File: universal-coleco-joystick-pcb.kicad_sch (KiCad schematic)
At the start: 45 parts, among them J1 Sanwa Joystick, J2 DE9_Receptacle, J3 Conn_01x09_Socket, SW1 Arm, SW10 2, SW11 #, SW12 9, SW13 6, SW14 3, SW2 Fire, SW3 *, SW4 7, SW5 1, SW6 4, SW7 0, SW8 8, SW9 5

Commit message: Diode soup
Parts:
- D1, D10, D11, D12, D13, D14, D15, D16, D17, D18, D19, D2, D20, D21, D22, D23, D24, D25, D26, D27, D28, D3, D4, D5, D6, D7, D8, D9: footprint (none) -> Diode_THT:D_DO-41_SOD81_P10.16mm_Horizontal
- J1: footprint (none) -> Connector_PinHeader_2.54mm:PinHeader_1x05_P2.54mm_Vertical
- J2: footprint (none) -> Connector_Dsub:DSUB-9_Female_Horizontal_P2.77x2.84mm_EdgePinOffset7.70mm_Housed_MountingHolesOffset9.12mm
- J3: footprint (none) -> Connector_PinHeader_2.54mm:PinHeader_1x09_P2.54mm_Vertical
- SW10, SW11, SW12, SW13, SW14, SW3, SW4, SW5, SW6, SW7, SW8, SW9: footprint (none) -> Connector_PinHeader_2.54mm:PinHeader_1x02_P2.54mm_Vertical
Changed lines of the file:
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@@
 			)
 		)
-		(property "Footprint" ""
+		(property "Footprint" "Diode_THT:D_DO-41_SOD81_P10.16mm_Horizontal"
 			(at 210.82 55.88 0)
 			(effects
@@
 			)
 		)
-		(property "Footprint" ""
+		(property "Footprint" "Diode_THT:D_DO-41_SOD81_P10.16mm_Horizontal"
 			(at 218.44 93.98 0)
 			(effects
@@
 			)
 		)
-		(property "Footprint" ""
+		(property "Footprint" "Diode_THT:D_DO-41_SOD81_P10.16mm_Horizontal"
 			(at 85.09 58.42 90)
 			(effects
@@
 			)
 		)
-		(property "Footprint" ""
+		(property "Footprint" "Diode_THT:D_DO-41_SOD81_P10.16mm_Horizontal"
 			(at 210.82 63.5 0)
 			(effects
@@
 			)
 		)
-		(property "Footprint" ""
+		(property "Footprint" "Diode_THT:D_DO-41_SOD81_P10.16mm_Horizontal"
 			(at 226.06 71.12 0)
 			(effects
@@
 			)
 		)
-		(property "Footprint" ""
+		(property "Footprint" "Diode_THT:D_DO-41_SOD81_P10.16mm_Horizontal"
 			(at 226.06 40.64 0)
 			(effects
@@
 			)
 		)
-		(property "Footprint" ""
+		(property "Footprint" "Diode_THT:D_DO-41_SOD81_P10.16mm_Horizontal"
 			(at 226.06 33.02 0)
 			(effects
@@
 			)
 		)
-		(property "Footprint" ""
+		(property "Footprint" "Diode_THT:D_DO-41_SOD81_P10.16mm_Horizontal"
 			(at 85.09 55.88 90)
 			(effects
@@
 			)
 		)
-		(property "Footprint" ""
+		(property "Footprint" "Diode_THT:D_DO-41_SOD81_P10.16mm_Horizontal"
 			(at 218.44 78.74 0)
 			(effects
@@
 			)
 		)
-		(property "Footprint" ""
+		(property "Footprint" "Diode_THT:D_DO-41_SOD81_P10.16mm_Horizontal"
 			(at 210.82 33.02 0)
 			(effects
@@
 			)
 		)
-		(property "Footprint" ""
+		(property "Footprint" "Connector_PinHeader_2.54mm:PinHeader_1x02_P2.54mm_Vertical"
 			(at 189.23 76.2 0)
 			(effects
@@
 			)
 		)
-		(property "Footprint" ""
+		(property "Footprint" "Connector_PinHeader_2.54mm:PinHeader_1x02_P2.54mm_Vertical"
 			(at 189.23 68.58 0)
 			(effects
@@
 			)
 		)
-		(property "Footprint" ""
+		(property "Footprint" "Connector_PinHeader_2.54mm:PinHeader_1x05_P2.54mm_Vertical"
 			(at 66.04 58.42 0)
 			(effects
@@
 			)
 		)
-		(property "Footprint" ""
+		(property "Footprint" "Diode_THT:D_DO-41_SOD81_P10.16mm_Horizontal"
 			(at 218.44 40.64 0)
 			(effects
@@
 			)
 		)
-		(property "Footprint" ""
+		(property "Footprint" "Connector_PinHeader_2.54mm:PinHeader_1x02_P2.54mm_Vertical"
 			(at 189.23 114.3 0)
 			(effects
@@
 			)
 		)
-		(property "Footprint" ""
+		(property "Footprint" "Connector_PinHeader_2.54mm:PinHeader_1x02_P2.54mm_Vertical"
 			(at 189.23 91.44 0)
 			(effects
@@
 			)
 		)
-		(property "Footprint" ""
+		(property "Footprint" "Connector_Dsub:DSUB-9_Female_Horizontal_P2.77x2.84mm_EdgePinOffset7.70mm_Housed_MountingHolesOffset9.12mm"
 			(at 96.52 143.51 0)
 			(effects
@@
 			)
 		)
-		(property "Footprint" ""
+		(property "Footprint" "Diode_THT:D_DO-41_SOD81_P10.16mm_Horizontal"
 			(at 80.01 78.74 90)
 			(effects
@@
 			)
 		)
-		(property "Footprint" ""
+		(property "Footprint" "Diode_THT:D_DO-41_SOD81_P10.16mm_Horizontal"
 			(at 203.2 109.22 0)
 			(effects
@@
 			)
 		)
-		(property "Footprint" ""
+		(property "Footprint" "Diode_THT:D_DO-41_SOD81_P10.16mm_Horizontal"
 			(at 226.06 116.84 0)
 			(effects
@@
 			)
 		)
-		(property "Footprint" ""
+		(property "Footprint" "Diode_THT:D_DO-41_SOD81_P10.16mm_Horizontal"
 			(at 218.44 71.12 0)
 			(effects
@@
 			)
 		)
-		(property "Footprint" ""
+		(property "Footprint" "Connector_PinHeader_2.54mm:PinHeader_1x09_P2.54mm_Vertical"
 			(at 48.26 163.83 0)
 			(effects
@@
 			)
 		)
-		(property "Footprint" ""
+		(property "Footprint" "Diode_THT:D_DO-41_SOD81_P10.16mm_Horizontal"
 			(at 210.82 71.12 0)
 			(effects
@@
 			)
 		)
-		(property "Footprint" ""
+		(property "Footprint" "Diode_THT:D_DO-41_SOD81_P10.16mm_Horizontal"
 			(at 218.44 86.36 0)
 			(effects
@@
 			)
 		)
-		(property "Footprint" ""
+		(property "Footprint" "Connector_PinHeader_2.54mm:PinHeader_1x02_P2.54mm_Vertical"
 			(at 189.23 106.68 0)
 			(effects
@@
 			)
 		)
-		(property "Footprint" ""
+		(property "Footprint" "Diode_THT:D_DO-41_SOD81_P10.16mm_Horizontal"
 			(at 218.44 55.88 0)
 			(effects
@@
 			)
 		)
-		(property "Footprint" ""
+		(property "Footprint" "Connector_PinHeader_2.54mm:PinHeader_1x02_P2.54mm_Vertical"
 			(at 189.23 53.34 0)
 			(effects
@@
 			)
 		)
-		(property "Footprint" ""
+		(property "Footprint" "Connector_PinHeader_2.54mm:PinHeader_1x02_P2.54mm_Vertical"
 			(at 189.23 60.96 0)
 			(effects
@@
 			)
 		)
-		(property "Footprint" ""
+		(property "Footprint" "Diode_THT:D_DO-41_SOD81_P10.16mm_Horizontal"
 			(at 210.82 78.74 0)
 			(effects
@@
 			)
 		)
-		(property "Footprint" ""
+		(property "Footprint" "Diode_THT:D_DO-41_SOD81_P10.16mm_Horizontal"
 			(at 85.09 60.96 90)
 			(effects
@@
 			)
 		)
-		(property "Footprint" ""
+		(property "Footprint" "Diode_THT:D_DO-41_SOD81_P10.16mm_Horizontal"
 			(at 226.06 48.26 0)
 			(effects
@@
 			)
 		)
-		(property "Footprint" ""
+		(property "Footprint" "Diode_THT:D_DO-41_SOD81_P10.16mm_Horizontal"
 			(at 203.2 116.84 0)
 			(effects
@@
 			)
 		)
-		(property "Footprint" ""
+		(property "Footprint" "Diode_THT:D_DO-41_SOD81_P10.16mm_Horizontal"
 			(at 80.01 91.44 90)
 			(effects
@@
 			)
 		)
-		(property "Footprint" ""
+		(property "Footprint" "Diode_THT:D_DO-41_SOD81_P10.16mm_Horizontal"
 			(at 85.09 53.34 90)
 			(effects
@@
 			)
 		)
-		(property "Footprint" ""
+		(property "Footprint" "Diode_THT:D_DO-41_SOD81_P10.16mm_Horizontal"
 			(at 210.82 101.6 0)
 			(effects
@@
 			)
 		)
-		(property "Footprint" ""
+		(property "Footprint" "Connector_PinHeader_2.54mm:PinHeader_1x02_P2.54mm_Vertical"
 			(at 189.23 38.1 0)
 			(effects
@@
 			)
 		)
-		(property "Footprint" ""
+		(property "Footprint" "Connector_PinHeader_2.54mm:PinHeader_1x02_P2.54mm_Vertical"
 			(at 189.23 83.82 0)
 			(effects
@@
 			)
 		)
-		(property "Footprint" ""
+		(property "Footprint" "Diode_THT:D_DO-41_SOD81_P10.16mm_Horizontal"
 			(at 203.2 63.5 0)
 			(effects
@@
 			)
 		)
-		(property "Footprint" ""
+		(property "Footprint" "Diode_THT:D_DO-41_SOD81_P10.16mm_Horizontal"
 			(at 203.2 93.98 0)
 			(effects
@@
 			)
 		)
-		(property "Footprint" ""
+		(property "Footprint" "Connector_PinHeader_2.54mm:PinHeader_1x02_P2.54mm_Vertical"
 			(at 189.23 99.06 0)
 			(effects
@@
 			)
 		)
-		(property "Footprint" ""
+		(property "Footprint" "Connector_PinHeader_2.54mm:PinHeader_1x02_P2.54mm_Vertical"
 			(at 189.23 30.48 0)
 			(effects
@@
 			)
 		)
-		(property "Footprint" ""
+		(property "Footprint" "Diode_THT:D_DO-41_SOD81_P10.16mm_Horizontal"
 			(at 203.2 55.88 0)
 			(effects
@@
 			)
 		)
-		(property "Footprint" ""
+		(property "Footprint" "Connector_PinHeader_2.54mm:PinHeader_1x02_P2.54mm_Vertical"
 			(at 189.23 45.72 0)
 			(effects

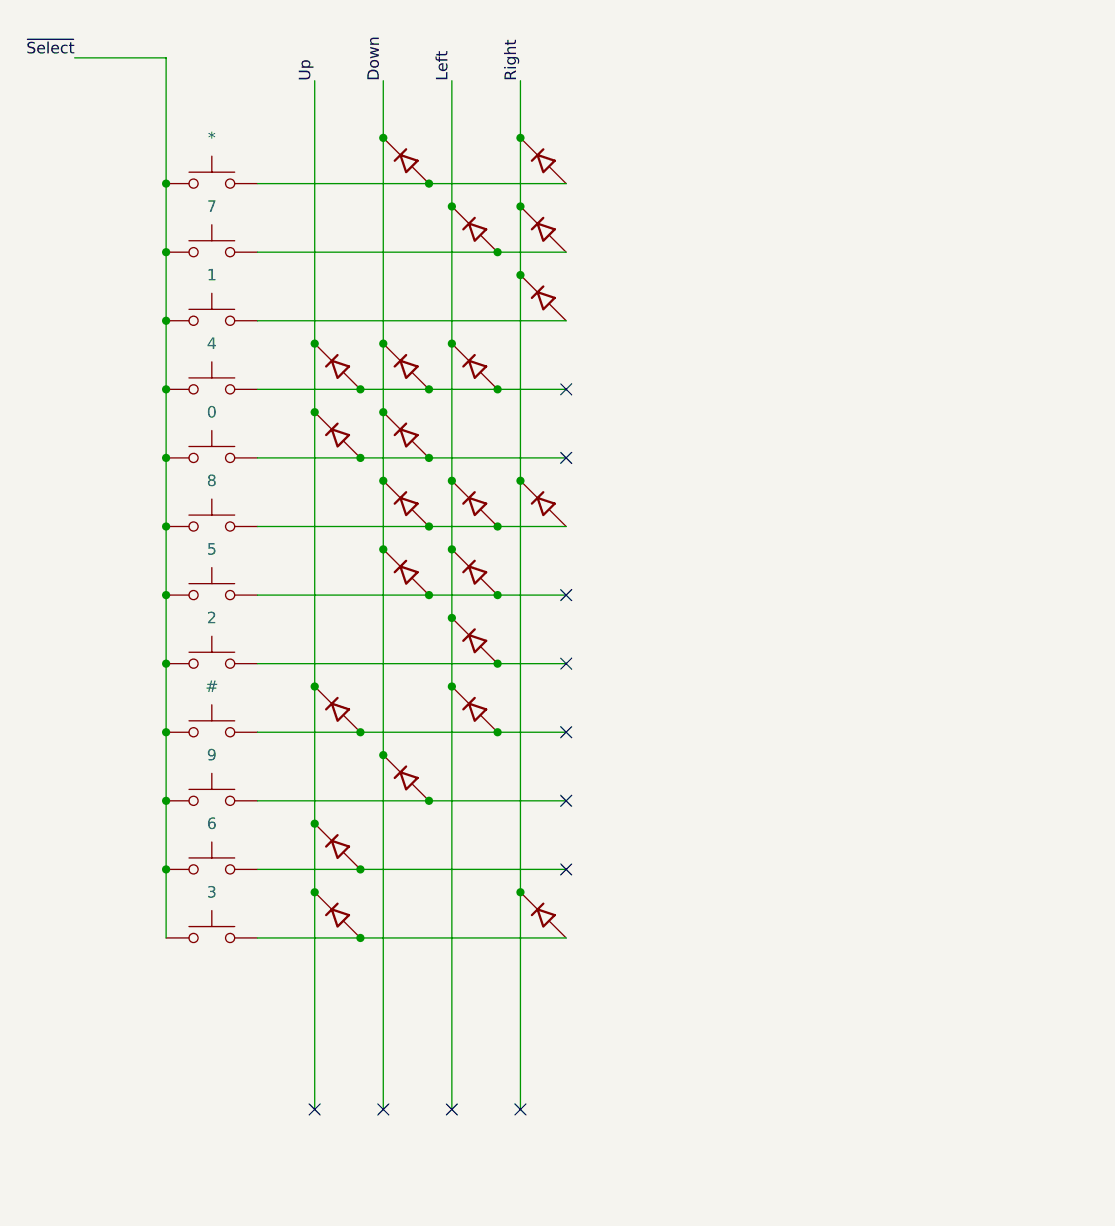
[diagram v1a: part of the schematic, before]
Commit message: Linear KP header
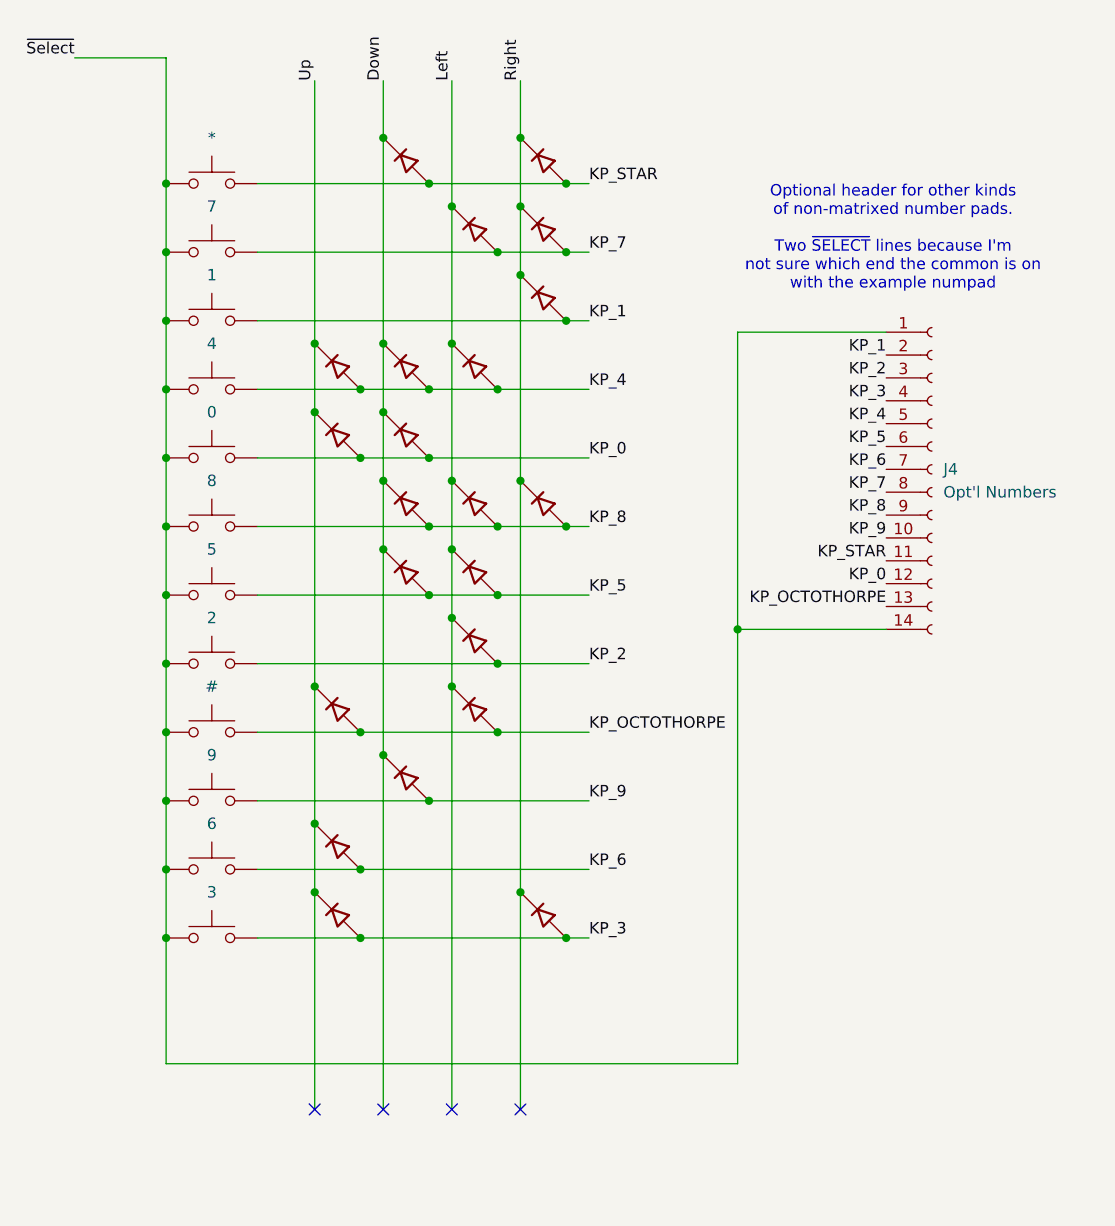
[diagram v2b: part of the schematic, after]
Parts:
- added J4: Opt'l Numbers, Connector_PinHeader_2.54mm:PinHeader_1x14_P2.54mm_Vertical, symbol Connector:Conn_01x14_Socket
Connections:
- net ~{Select}: now also J4.1 (Pin_1), J4.14 (Pin_14)
- net KP_4: now reaches D12.2 (A), D13.2 (A), D14.2 (A), SW6.2
- net KP_4: now also J4.5 (Pin_5)
- net KP_OCTOTHORPE: now reaches D23.2 (A), D24.2 (A), SW11.2
- net KP_OCTOTHORPE: now also J4.13 (Pin_13)
- net KP_0: now reaches D15.2 (A), D16.2 (A), SW7.2
- net KP_0: now also J4.12 (Pin_12)
- net KP_8: now reaches D17.2 (A), D18.2 (A), D19.2 (A), SW8.2
- net KP_8: now also J4.9 (Pin_9)
- net KP_7: now reaches D10.2 (A), D9.2 (A), SW4.2
- net KP_7: now also J4.8 (Pin_8)
- net KP_STAR: now reaches D7.2 (A), D8.2 (A), SW3.2
- net KP_STAR: now also J4.11 (Pin_11)
- net KP_5: now reaches D20.2 (A), D21.2 (A), SW9.2
- net KP_5: now also J4.6 (Pin_6)
- net KP_3: now reaches D27.2 (A), D28.2 (A), SW14.2
- net KP_3: now also J4.4 (Pin_4)
- net KP_6: now reaches D26.2 (A), SW13.2
- net KP_6: now also J4.7 (Pin_7)
- net KP_2: now reaches D22.2 (A), SW10.2
- net KP_2: now also J4.3 (Pin_3)
- net KP_1: now reaches D11.2 (A), SW5.2
- net KP_1: now also J4.2 (Pin_2)
- net KP_9: now reaches D25.2 (A), SW12.2
- net KP_9: now also J4.10 (Pin_10)
- no-connect marks 11 -> 4
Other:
- note added: "Optional header for other kinds of non-matrixed number pads. Two ~{SELECT} lines because I'm not sure which end the common is on with the example numpad"

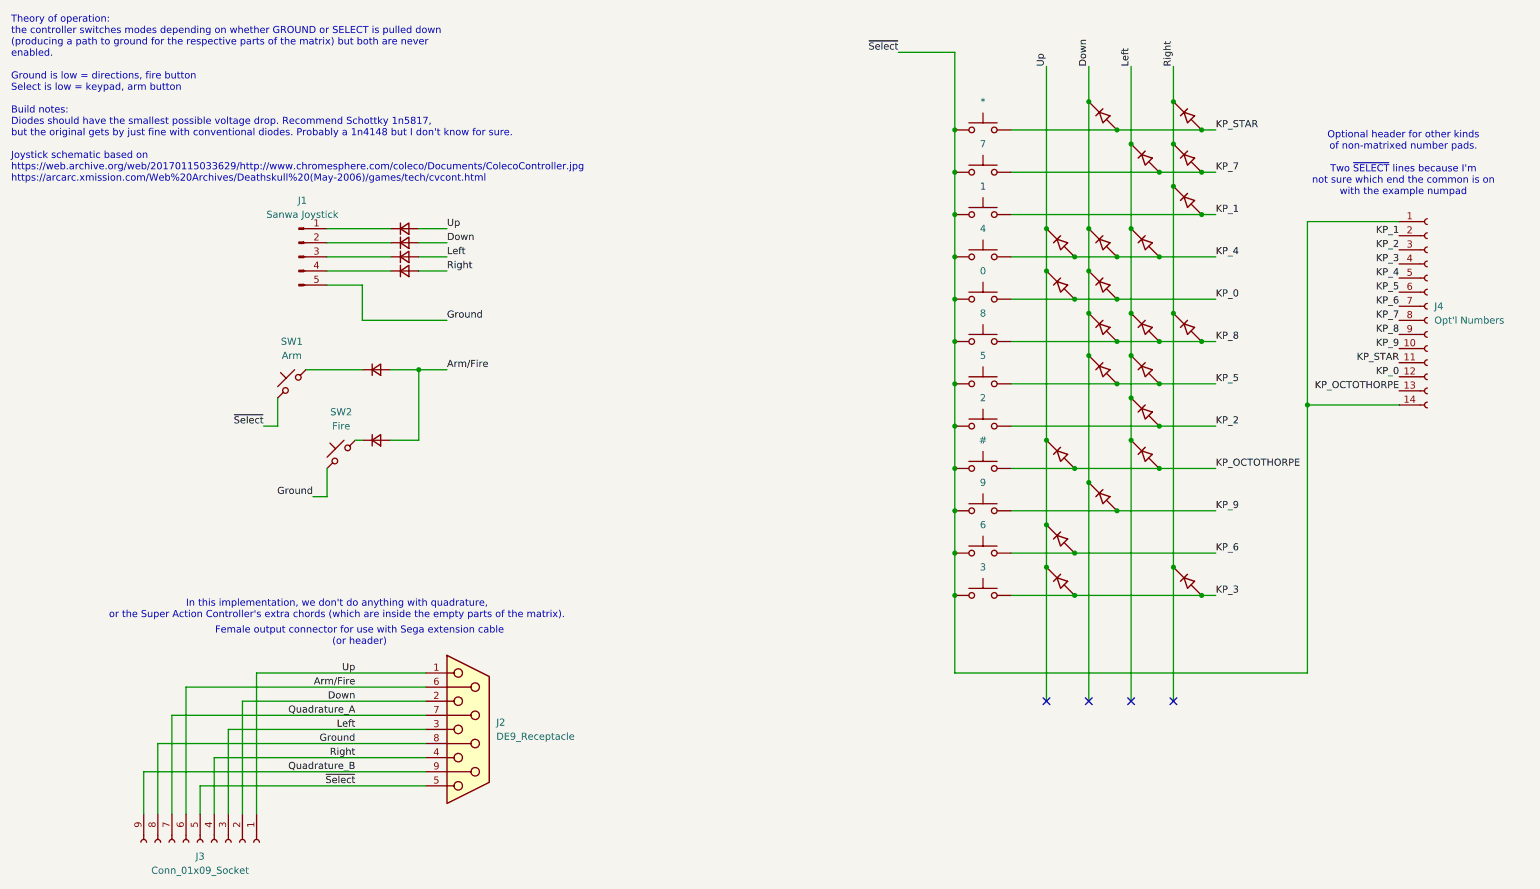
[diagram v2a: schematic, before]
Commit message: Warning: Diodes may be backward for number matrix
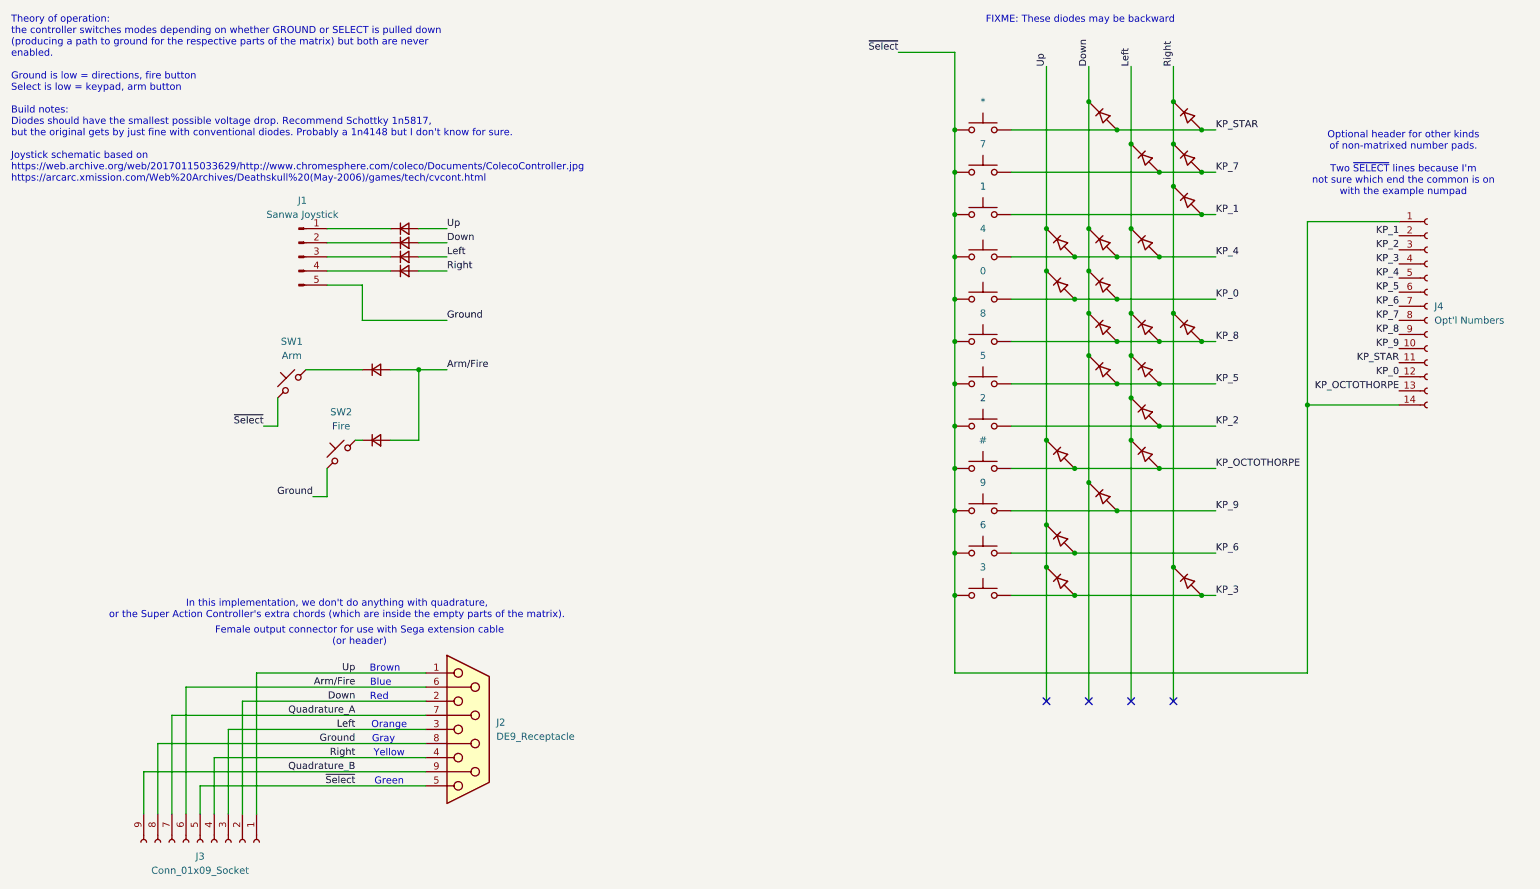
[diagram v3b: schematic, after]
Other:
- note added: "Blue"
- note added: "Brown"
- note added: "FIXME: These diodes may be backward"
- note added: "Gray"
- note added: "Green"
- note added: "Orange"
- note added: "Red"
- note added: "Yellow"
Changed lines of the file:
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@@
+		)
+	)
+	(text "Green"
+		(exclude_from_sim no)
+		(at 82.296 152.908 0)
+		(effects
+			(font
+				(size 1.27 1.27)
+			)
+		)
+	)
+	(text "Blue"
+		(exclude_from_sim no)
+		(at 80.772 135.128 0)
+		(effects
+			(font
+				(size 1.27 1.27)
+			)
+		)
+	)
+	(text "Brown"
+		(exclude_from_sim no)
+		(at 81.534 132.588 0)
+		(effects
+			(font
+				(size 1.27 1.27)
+			)
 		)
 	)
@@
 		)
 	)
+	(text "Red"
+		(exclude_from_sim no)
+		(at 80.518 137.668 0)
+		(effects
+			(font
+				(size 1.27 1.27)
+			)
+		)
+	)
 	(text "In this implementation, we don't do anything with quadrature,\nor the Super Action Controller's extra chords (which are inside the empty parts of the matrix)."
 		(exclude_from_sim no)
 		(at 72.898 121.92 0)
+		(effects
+			(font
+				(size 1.27 1.27)
+			)
+		)
+	)
+	(text "FIXME: These diodes may be backward"
+		(exclude_from_sim no)
+		(at 206.756 15.748 0)
+		(effects
+			(font
+				(size 1.27 1.27)
+			)
+		)
+	)
+	(text "Yellow"
+		(exclude_from_sim no)
+		(at 82.296 147.828 0)
+		(effects
+			(font
+				(size 1.27 1.27)
+			)
+		)
+	)
+	(text "Gray"
+		(exclude_from_sim no)
+		(at 81.28 145.288 0)
+		(effects
+			(font
+				(size 1.27 1.27)
+			)
+		)
+	)
+	(text "Orange"
+		(exclude_from_sim no)
+		(at 82.296 142.748 0)
 		(effects
 			(font
@@
 		(on_board yes)
 		(dnp no)
-		(fields_autoplaced yes)
 		(property "Reference" "D8"
 			(at 226.06 27.94 0)
@@
 		(on_board yes)
 		(dnp no)
-		(fields_autoplaced yes)
 		(property "Reference" "D7"
 			(at 210.82 27.94 0)
